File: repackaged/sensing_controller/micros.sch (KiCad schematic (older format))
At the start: 27 parts

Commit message: Work on micros.sch
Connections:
- net CS3.3V: no longer U?.14 ((PCINT2/~SS~/OC1B)PB2)
- net POT_MICRO_SENSE: now reaches U?.23 ((ADC0/PCINT8)PC0)
- net SCL renamed SM_SCL
- net SDA renamed SM_SDA
- new net SM_CS: U?.14 ((PCINT2/~SS~/OC1B)PB2)
- no-connect marks 25 -> 24
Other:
- moved on the sheet: C?, Y?
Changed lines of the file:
@@
 $EndDescr
 Text Label 9610 1550 0    50   ~ 0
-CS3.3V
+SM_CS
 Text Label 7570 980  0    50   ~ 0
 3.3V
@@
 NoConn ~ 9610 2450
 NoConn ~ 9610 2350
-NoConn ~ 9610 2250
 Wire Wire Line
 	7570 1650 7570 2520
@@
 Text Label 9610 1850 0    50   ~ 0
 SM_SCK
-Text Label 9610 2750 0    50   ~ 0
-SCL
-Text Label 9610 2650 0    50   ~ 0
-SDA
 Wire Wire Line
 	9900 2850 9610 2850
@@
 L power:GND #PWR?
 U 1 1 60A51E4F
-P 10590 1940
-F 0 "#PWR?" H 10590 1690 50  0001 C CNN
-F 1 "GND" H 10595 1767 50  0000 C CNN
-F 2 "" H 10590 1940 50  0001 C CNN
-F 3 "" H 10590 1940 50  0001 C CNN
-	1    10590 1940
+P 10980 1940
+F 0 "#PWR?" H 10980 1690 50  0001 C CNN
+F 1 "GND" H 10985 1767 50  0000 C CNN
+F 2 "" H 10980 1940 50  0001 C CNN
+F 3 "" H 10980 1940 50  0001 C CNN
+	1    10980 1940
 	1    0    0    -1
 $EndComp
@@
 L power:GND #PWR?
 U 1 1 60A51E5E
+P 10700 2660
+F 0 "#PWR?" H 10700 2410 50  0001 C CNN
+F 1 "GND" H 10705 2487 50  0000 C CNN
+F 2 "" H 10700 2660 50  0001 C CNN
+F 3 "" H 10700 2660 50  0001 C CNN
+	1    10700 2660
+	1    0    0    -1
+$EndComp
+$Comp
+L power:GND #PWR?
+U 1 1 60A51E64
 P 10310 2660
 F 0 "#PWR?" H 10310 2410 50  0001 C CNN
@@
 $EndComp
 $Comp
-L power:GND #PWR?
-U 1 1 60A51E64
-P 9910 2660
-F 0 "#PWR?" H 9910 2410 50  0001 C CNN
-F 1 "GND" H 9915 2487 50  0000 C CNN
-F 2 "" H 9910 2660 50  0001 C CNN
-F 3 "" H 9910 2660 50  0001 C CNN
-	1    9910 2660
-	1    0    0    -1
-$EndComp
-$Comp
 L formula:C_30pF C?
 U 1 1 60A51E6D
-P 10310 2510
-F 0 "C?" H 10330 2590 50  0000 L CNN
-F 1 "C_30pF" H 10340 2410 50  0000 L CNN
-F 2 "footprints:C_0805_OEM" H 10348 2360 50  0001 C CNN
-F 3 "https://media.digikey.com/pdf/Data%20Sheets/Samsung%20PDFs/CL_Series_MLCC_ds.pdf" H 10335 2610 50  0001 C CNN
-F 4 "DK" H 10310 2510 60  0001 C CNN "MFN"
-F 5 "1276-1130-1-ND" H 10310 2510 60  0001 C CNN "MPN"
-F 6 "https://www.digikey.com/product-detail/en/samsung-electro-mechanics-america-inc/CL21C300JBANNNC/1276-1130-1-ND/3889216" H 10735 3010 60  0001 C CNN "PurchasingLink"
-	1    10310 2510
-	1    0    0    -1
-$EndComp
-$Comp
-L formula:C_30pF C?
-U 1 1 60A51E76
-P 9910 2510
-F 0 "C?" H 9800 2590 50  0000 L CNN
-F 1 "C_30pF" H 9640 2430 50  0000 L CNN
-F 2 "footprints:C_0805_OEM" H 9948 2360 50  0001 C CNN
-F 3 "https://media.digikey.com/pdf/Data%20Sheets/Samsung%20PDFs/CL_Series_MLCC_ds.pdf" H 9935 2610 50  0001 C CNN
-F 4 "DK" H 9910 2510 60  0001 C CNN "MFN"
-F 5 "1276-1130-1-ND" H 9910 2510 60  0001 C CNN "MPN"
-F 6 "https://www.digikey.com/product-detail/en/samsung-electro-mechanics-america-inc/CL21C300JBANNNC/1276-1130-1-ND/3889216" H 10335 3010 60  0001 C CNN "PurchasingLink"
-	1    9910 2510
-	1    0    0    -1
-$EndComp
-$Comp
-L formula:Crystal_SMD Y?
-U 1 1 60A51E7F
-P 10130 2270
-F 0 "Y?" H 10274 2316 50  0000 L CNN
-F 1 "Crystal_SMD" H 10274 2225 50  0000 L CNN
-F 2 "footprints:Crystal_SMD_FA238" H 10080 2345 50  0001 C CNN
-F 3 "http://www.txccorp.com/download/products/quartz_crystals/2015TXC_7M_17.pdf" H 10180 2445 50  0001 C CNN
-F 4 "DK" H 10130 2270 60  0001 C CNN "MFN"
-F 5 "887-1125-1-ND" H 10130 2270 60  0001 C CNN "MPN"
-F 6 "https://www.digikey.com/product-detail/en/txc-corporation/7M-16.000MAAJ-T/887-1125-1-ND/2119014" H 10580 2845 60  0001 C CNN "PurchasingLink"
-	1    10130 2270
-	1    0    0    -1
-$EndComp
-Wire Wire Line
-	9910 2050 9910 2270
-Wire Wire Line
-	10310 1950 10310 2270
-Wire Wire Line
-	10030 2270 9910 2270
-Connection ~ 9910 2270
-Wire Wire Line
-	9910 2270 9910 2360
-Wire Wire Line
-	10230 2270 10310 2270
-Connection ~ 10310 2270
-Wire Wire Line
-	10310 2270 10310 2360
-$Comp
-L power:GND #PWR?
-U 1 1 60A51E8D
-P 10130 2420
-F 0 "#PWR?" H 10130 2170 50  0001 C CNN
-F 1 "GND" H 10135 2247 50  0000 C CNN
-F 2 "" H 10130 2420 50  0001 C CNN
-F 3 "" H 10130 2420 50  0001 C CNN
-	1    10130 2420
-	1    0    0    -1
-$EndComp
-Wire Wire Line
-	9610 2050 9910 2050
-Wire Wire Line
-	10310 1950 9610 1950
-Wire Wire Line
-	10130 1740 10130 2120
-Wire Wire Line
-	10130 1740 10590 1740
-Wire Wire Line
-	10590 1740 10590 1940
+P 10700 2510
+F 0 "C?" H 10720 2590 50  0000 L CNN
+F 1 "C_30pF" H 10730 2410 50  0000 L CNN
+F 2 "footprints:C_0805_OEM" H 10738 2360 50  0001 C CNN
+F 3 "https://media.digikey.com/pdf/Data%20Sheets/Samsung%20PDFs/CL_Series_MLCC_ds.pdf" H 10725 2610 50  0001 C CNN
+F 4 "DK" H 10700 2510 60  0001 C CNN "MFN"
+F 5 "1276-1130-1-ND" H 10700 2510 60  0001 C CNN "MPN"
+F 6 "https://www.digikey.com/product-detail/en/samsung-electro-mechanics-america-inc/CL21C300JBANNNC/1276-1130-1-ND/3889216" H 11125 3010 60  0001 C CNN "PurchasingLink"
+	1    10700 2510
+	1    0    0    -1
+$EndComp
+Wire Wire Line
+	10700 1950 10700 2270
+Wire Wire Line
+	10620 2270 10700 2270
+Connection ~ 10700 2270
+Wire Wire Line
+	10700 2270 10700 2360
+Wire Wire Line
+	10520 1740 10980 1740
+Wire Wire Line
+	10980 1740 10980 1940
 Wire Wire Line
 	8010 3450 7740 3450
@@
 	1050 1100 1350 1100
 Connection ~ 1050 1400
+Text GLabel 9610 2250 2    50   Input ~ 0
+POT_MICRO_SENSE
+Wire Wire Line
+	10310 2050 10310 2270
+$Comp
+L formula:Crystal_SMD Y?
+U 1 1 60A51E7F
+P 10520 2270
+F 0 "Y?" H 10664 2316 50  0000 L CNN
+F 1 "Crystal_SMD" H 10664 2225 50  0000 L CNN
+F 2 "footprints:Crystal_SMD_FA238" H 10470 2345 50  0001 C CNN
+F 3 "http://www.txccorp.com/download/products/quartz_crystals/2015TXC_7M_17.pdf" H 10570 2445 50  0001 C CNN
+F 4 "DK" H 10520 2270 60  0001 C CNN "MFN"
+F 5 "887-1125-1-ND" H 10520 2270 60  0001 C CNN "MPN"
+F 6 "https://www.digikey.com/product-detail/en/txc-corporation/7M-16.000MAAJ-T/887-1125-1-ND/2119014" H 10970 2845 60  0001 C CNN "PurchasingLink"
+	1    10520 2270
+	1    0    0    -1
+$EndComp
+Wire Wire Line
+	10520 1740 10520 2120
+$Comp
+L power:GND #PWR?
+U 1 1 60A51E8D
+P 10520 2420
+F 0 "#PWR?" H 10520 2170 50  0001 C CNN
+F 1 "GND" H 10525 2247 50  0000 C CNN
+F 2 "" H 10520 2420 50  0001 C CNN
+F 3 "" H 10520 2420 50  0001 C CNN
+	1    10520 2420
+	1    0    0    -1
+$EndComp
+$Comp
+L formula:C_30pF C?
+U 1 1 60A51E76
+P 10310 2510
+F 0 "C?" H 10200 2590 50  0000 L CNN
+F 1 "C_30pF" H 10040 2430 50  0000 L CNN
+F 2 "footprints:C_0805_OEM" H 10348 2360 50  0001 C CNN
+F 3 "https://media.digikey.com/pdf/Data%20Sheets/Samsung%20PDFs/CL_Series_MLCC_ds.pdf" H 10335 2610 50  0001 C CNN
+F 4 "DK" H 10310 2510 60  0001 C CNN "MFN"
+F 5 "1276-1130-1-ND" H 10310 2510 60  0001 C CNN "MPN"
+F 6 "https://www.digikey.com/product-detail/en/samsung-electro-mechanics-america-inc/CL21C300JBANNNC/1276-1130-1-ND/3889216" H 10735 3010 60  0001 C CNN "PurchasingLink"
+	1    10310 2510
+	1    0    0    -1
+$EndComp
+Wire Wire Line
+	10430 2270 10420 2270
+Connection ~ 10310 2270
+Wire Wire Line
+	10310 2270 10310 2360
+Connection ~ 10420 2270
+Wire Wire Line
+	10420 2270 10310 2270
+Wire Wire Line
+	9610 1950 10700 1950
+Wire Wire Line
+	9610 2050 10310 2050
+Text GLabel 9610 2650 2    50   Input ~ 0
+SM_SDA
+Text GLabel 9610 2750 2    50   Input ~ 0
+SM_SCL
 $EndSCHEMATC

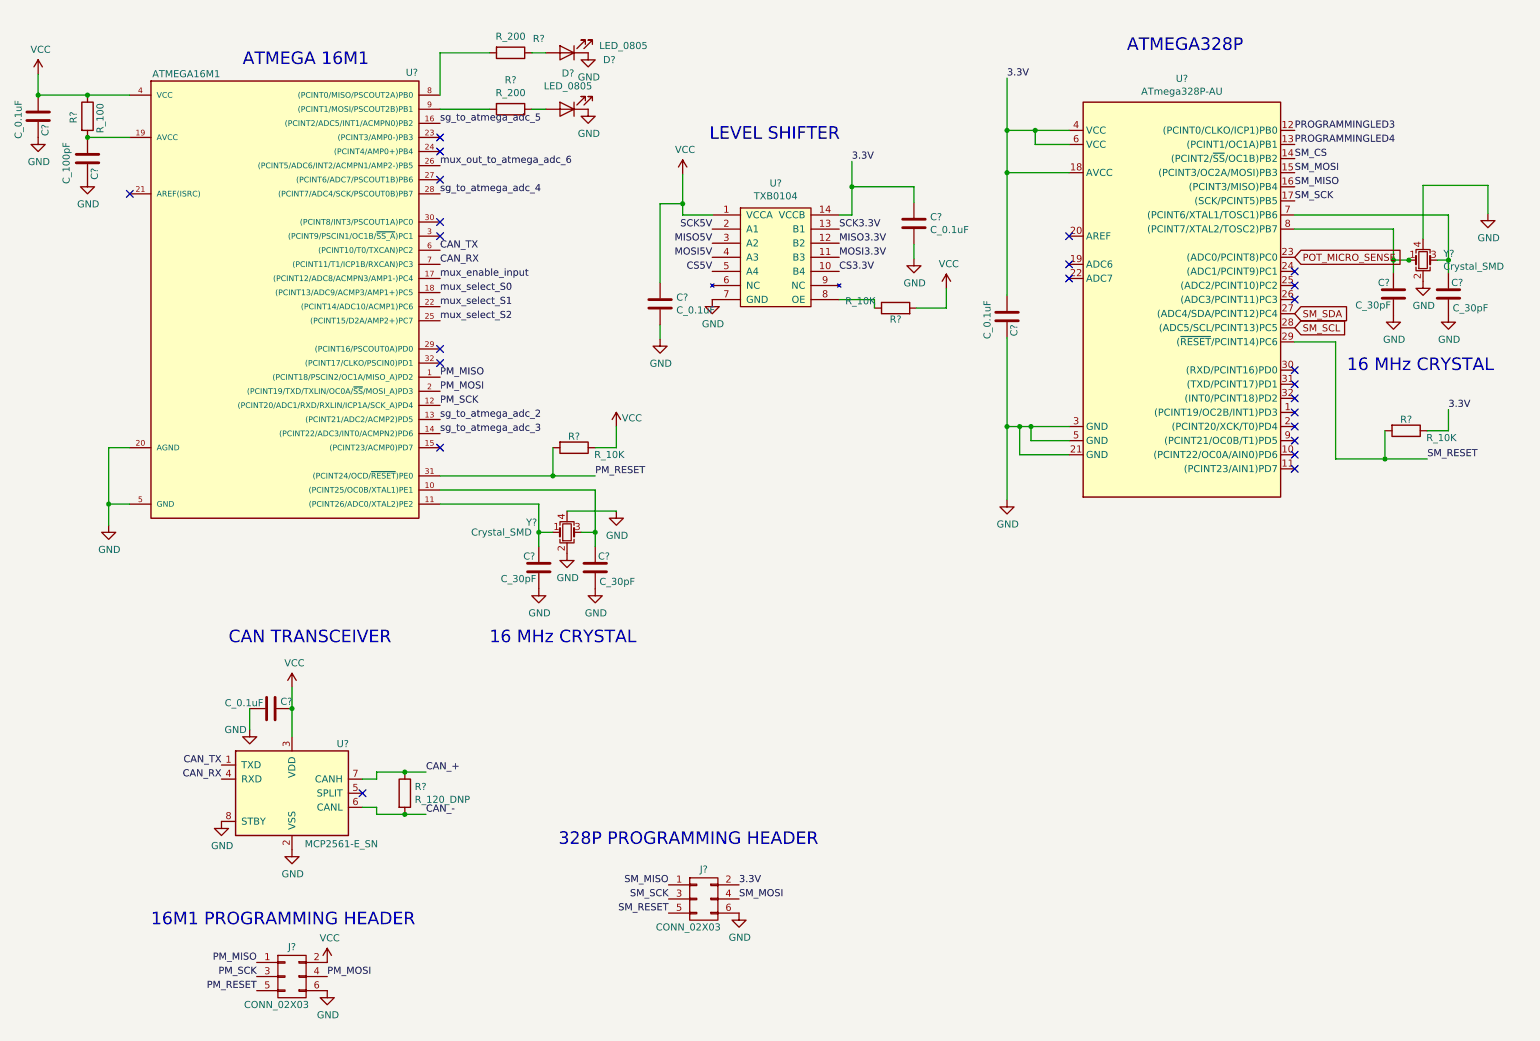
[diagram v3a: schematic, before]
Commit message: Changed micro board to be less cramped, and added global labels.
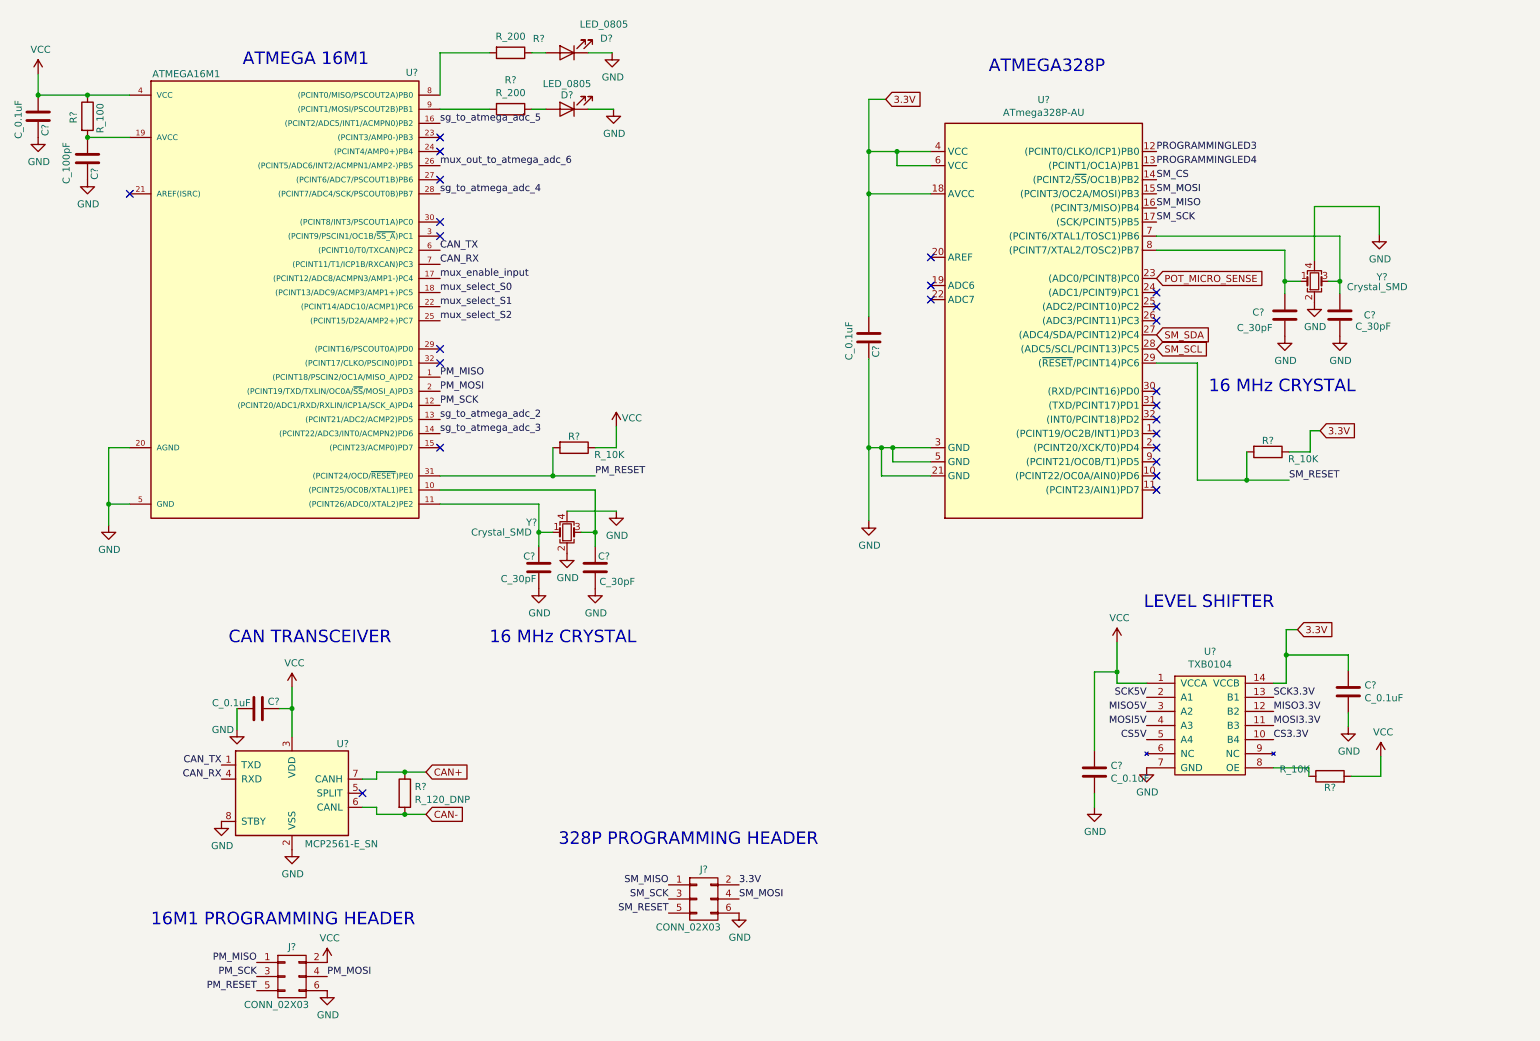
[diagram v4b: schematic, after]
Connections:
- net CAN_+ renamed CAN+
- net CAN_- renamed CAN-
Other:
- moved on the sheet: C?, R?, U?, Y?

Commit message: Annotate micros sheet.
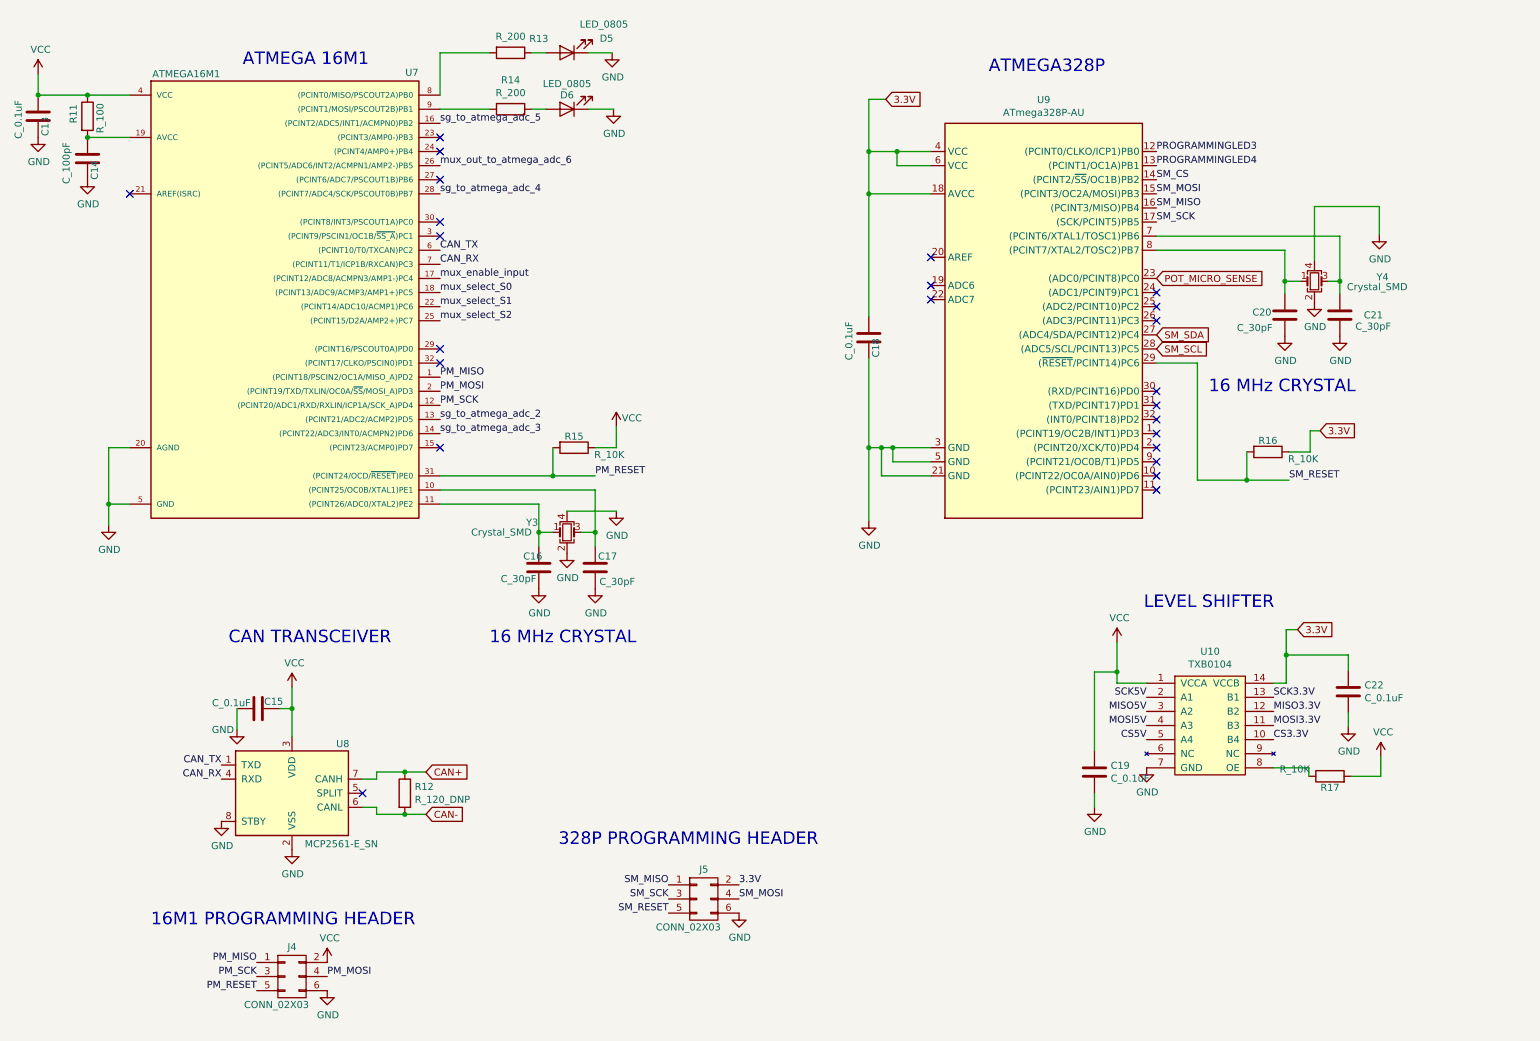
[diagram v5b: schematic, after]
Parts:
- gave numbers to parts that had none: 27

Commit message: Change vcc to +5V and fix net labels.
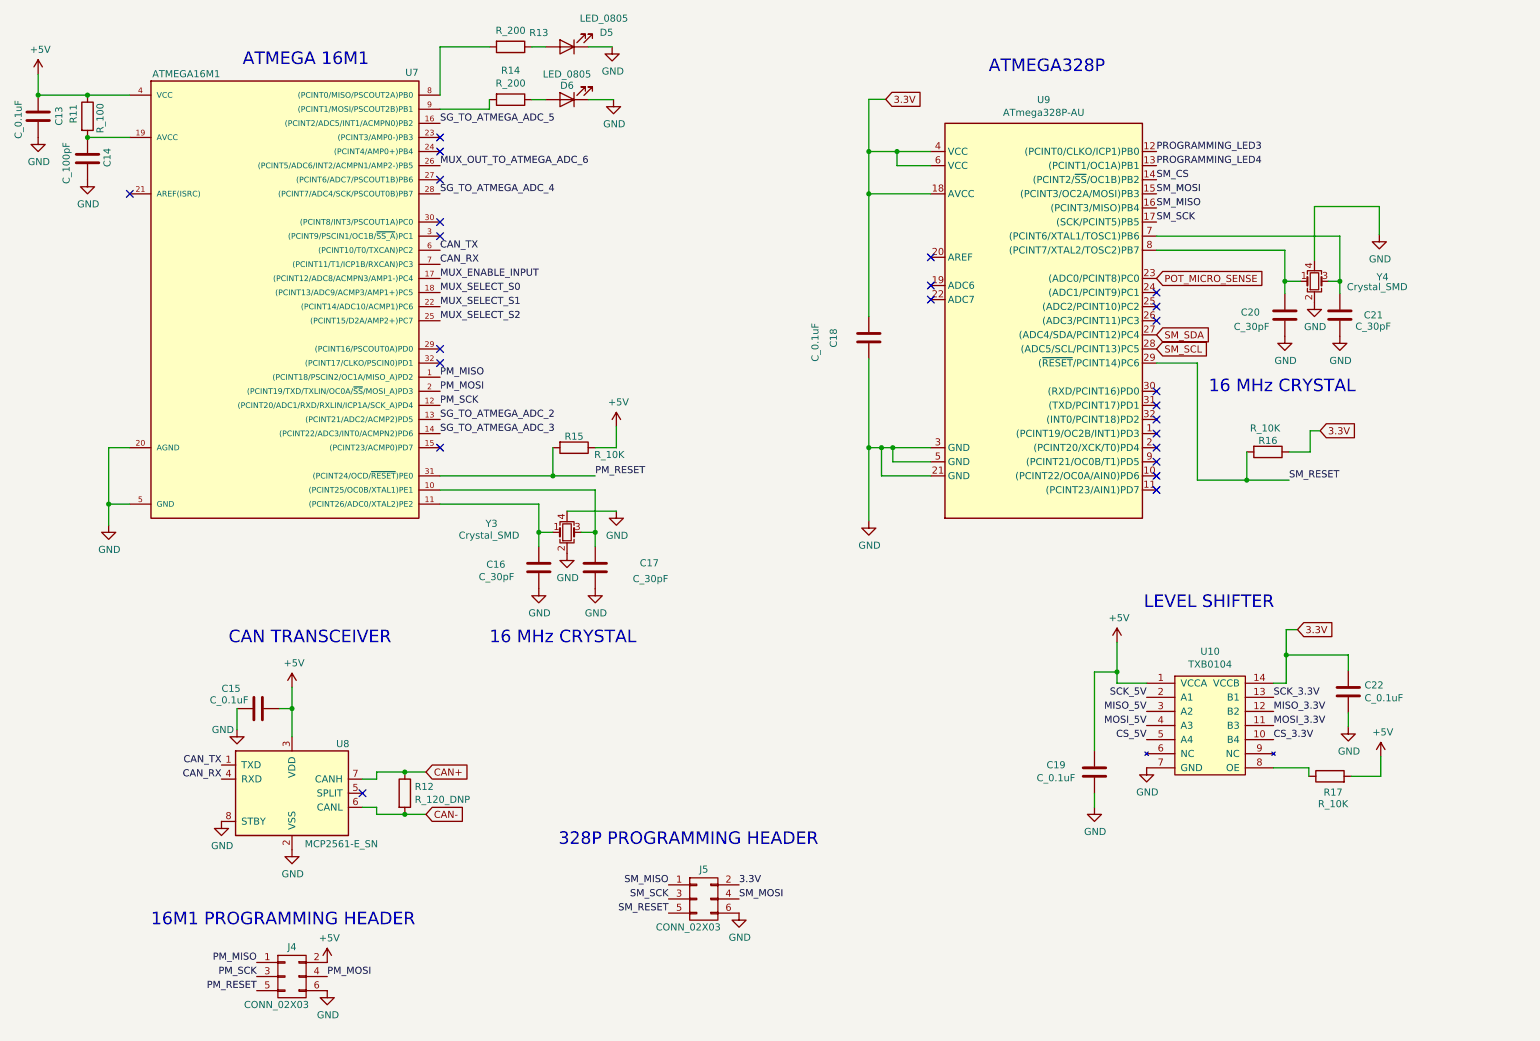
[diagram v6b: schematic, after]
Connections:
- net CS3.3V renamed CS_3.3V
- net CS5V renamed CS_5V
- net MISO3.3V renamed MISO_3.3V
- net MISO5V renamed MISO_5V
- net MOSI3.3V renamed MOSI_3.3V
- net MOSI5V renamed MOSI_5V
- net PROGRAMMINGLED3 renamed PROGRAMMING_LED3
- net PROGRAMMINGLED4 renamed PROGRAMMING_LED4
- net SCK3.3V renamed SCK_3.3V
- net SCK5V renamed SCK_5V
- net VCC renamed +5V
- net mux_enable_input renamed MUX_ENABLE_INPUT
- net mux_out_to_atmega_adc_6 renamed MUX_OUT_TO_ATMEGA_ADC_6
- net mux_select_S0 renamed MUX_SELECT_S0
- net mux_select_S1 renamed MUX_SELECT_S1
- net mux_select_S2 renamed MUX_SELECT_S2
- net sg_to_atmega_adc_2 renamed SG_TO_ATMEGA_ADC_2
- net sg_to_atmega_adc_3 renamed SG_TO_ATMEGA_ADC_3
- net sg_to_atmega_adc_4 renamed SG_TO_ATMEGA_ADC_4
- net sg_to_atmega_adc_5 renamed SG_TO_ATMEGA_ADC_5
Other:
- moved on the sheet: D5, D6, R13, R14
